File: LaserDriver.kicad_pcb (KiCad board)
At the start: 2 copper layers, 40.2 x 40.5 mm, 30 parts, among them J100 Screw_Terminal_01x04, J101 Screw_Terminal_01x02, J102 nano_left, J103 nano_right, U100 TPS92513DGQR

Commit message: added poors for ground
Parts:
- moved R104 0.83 mm to (49.2, 111.6)
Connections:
- net Net-(C106-Pad1) renamed /intersection
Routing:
- net GND: track 39.1 -> 15.2 mm, vias 18 -> 14
- net /intersection: track 6.43 -> 0.00 mm
- net /ard_DAC: track 4.96 -> 1.94 mm
- net /DAC: track 3.73 -> 2.28 mm
- net Net-(U100-ISENSE): track 2.44 -> 3.26 mm
- added copper zone on F.Cu, net /DAC
- added copper zone on F.Cu, net /ard_DAC
- added copper zone on F.Cu, net /intersection
- added copper zone on F.Cu, net GND

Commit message: added silkscreen and logo
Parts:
- added G***: LOGO, LOGO, F.Cu at (49.6, 125.5)
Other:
- board text added: "DCCD v1.0"
- board text added: "lighteye.ch"

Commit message: created calculator sheets
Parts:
- D101: value D_Zener -> D_Schottky
- moved D101 0.14 mm to (46.0, 104.8)

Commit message: created gerber and assembly files
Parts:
- moved D101 0.25 mm to (46.2, 104.8)
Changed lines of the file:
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@@
 			(usegerberattributes yes)
 			(usegerberadvancedattributes yes)
-			(creategerberjobfile yes)
+			(creategerberjobfile no)
 			(dashed_line_dash_ratio 12.000000)
 			(dashed_line_gap_ratio 3.000000)
@@
 			(outputformat 1)
 			(mirror no)
-			(drillshape 1)
+			(drillshape 0)
 			(scaleselection 1)
-			(outputdirectory "")
+			(outputdirectory "Gerbers/")
 		)
 	)
@@
 	(footprint "Diode_SMD:D_SMB"
 		(layer "F.Cu")
-		(at 46 104.8 90)
+		(at 46.25 104.8 90)
 		(descr "Diode SMB (DO-214AA)")
 		(tags "Diode SMB (DO-214AA)")
@@
 	)
 	(via
-		(at 46.05 99.675)
+		(at 46.3 99.675)
 		(size 1.6)
 		(drill 0.8)
@@
 	)
 	(segment
-		(start 47.31 106.95)
-		(end 49.825 104.435)
+		(start 43.66 106.95)
+		(end 42.825 107.785)
 		(width 0.7)
 		(layer "F.Cu")
@@
 	)
 	(segment
-		(start 46 106.95)
-		(end 43.66 106.95)
+		(start 46.25 106.95)
+		(end 46 107.2)
 		(width 0.7)
 		(layer "F.Cu")
@@
 	)
 	(segment
-		(start 43.66 106.95)
-		(end 42.825 107.785)
+		(start 46 108.626498)
+		(end 45.467501 109.158997)
 		(width 0.7)
 		(layer "F.Cu")
@@
 	)
 	(segment
-		(start 46 106.95)
-		(end 47.31 106.95)
+		(start 47.31 106.95)
+		(end 46.25 106.95)
 		(width 0.7)
 		(layer "F.Cu")
@@
 	)
 	(segment
-		(start 46 106.95)
+		(start 46 107.2)
 		(end 46 108.626498)
 		(width 0.7)
@@
 	)
 	(segment
-		(start 46 108.626498)
-		(end 45.467501 109.158997)
+		(start 49.825 104.435)
+		(end 47.31 106.95)
+		(width 0.7)
+		(layer "F.Cu")
+		(net 4)
+	)
+	(segment
+		(start 46.25 106.95)
+		(end 43.66 106.95)
 		(width 0.7)
 		(layer "F.Cu")
@@
 		(polygon
 			(pts
-				(xy 47.25 104) (xy 44.75 104) (xy 44.75 101.25) (xy 45.5 99.15) (xy 46.55 99.15) (xy 47.25 101.25)
+				(xy 47.5 104) (xy 45 104) (xy 45 101.25) (xy 45.75 99.15) (xy 46.8 99.15) (xy 47.5 101.25)
 			)
 		)

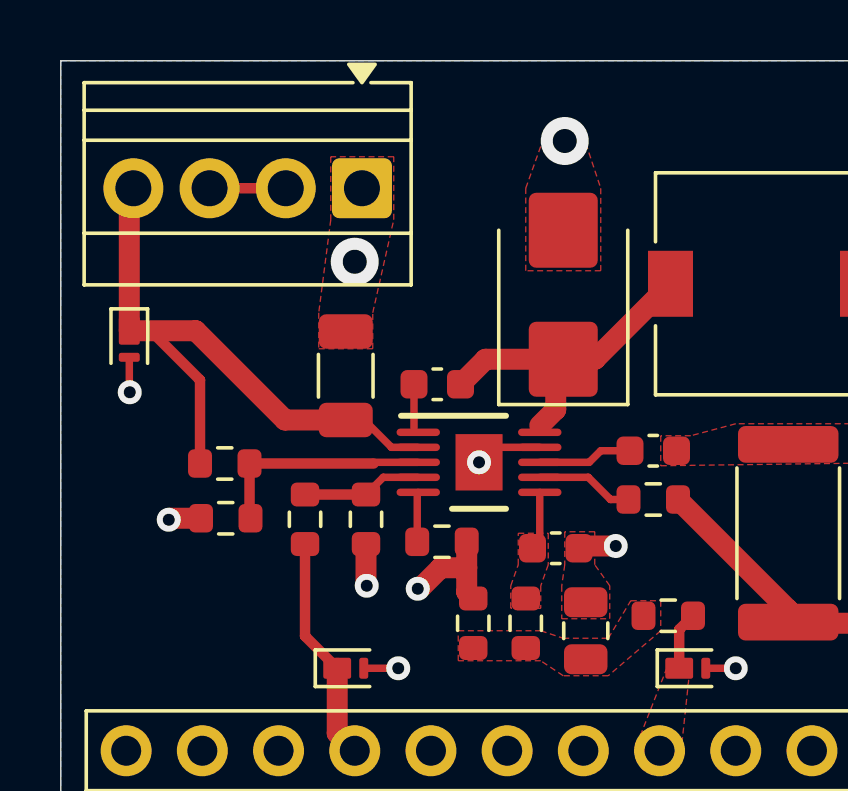
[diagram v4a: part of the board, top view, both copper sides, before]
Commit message: changes to tps ground via
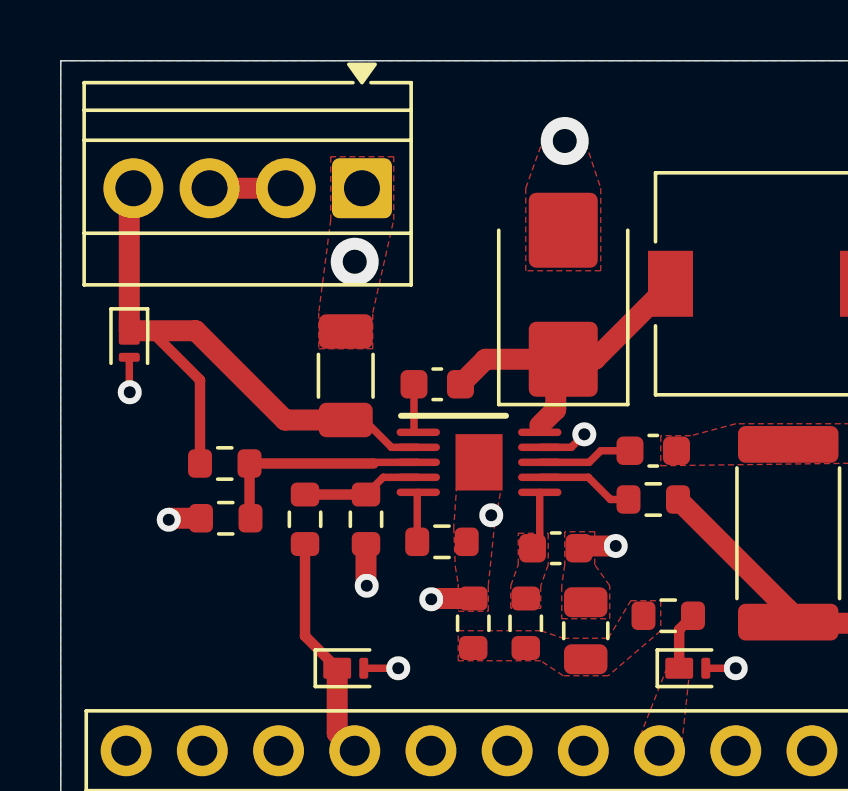
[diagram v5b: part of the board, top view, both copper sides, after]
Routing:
- net GND: track 15.2 -> 12.8 mm, vias 14 -> 15
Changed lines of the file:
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@@
 			(plotpadnumbers no)
 			(hidednponfab no)
-			(sketchdnponfab yes)
-			(crossoutdnponfab yes)
+			(sketchdnponfab no)
+			(crossoutdnponfab no)
 			(subtractmaskfromsilk no)
 			(outputformat 1)
@@
 		)
 		(fp_line
-			(start -0.900001 1.549999)
-			(end 0.900001 1.549999)
-			(stroke
-				(width 0.2)
-				(type solid)
-			)
-			(layer "F.SilkS")
-		)
-		(fp_line
 			(start -2.849999 -1.650002)
 			(end 2.849999 -1.650002)
@@
 	)
 	(segment
-		(start 45.467501 109.884997)
-		(end 43.942503 109.884997)
-		(width 0.25)
-		(layer "F.Cu")
-		(net 1)
-	)
-	(segment
 		(start 31.785 108.035)
 		(end 31.8 108.05)
@@
 	)
 	(segment
-		(start 43.0325 114.7075)
-		(end 43.25 114.925)
-		(width 0.7)
-		(layer "F.Cu")
-		(net 1)
-	)
-	(segment
-		(start 41.4675 114.6)
-		(end 41.4 114.6)
+		(start 48 113.175)
+		(end 46.85 113.175)
 		(width 0.7)
 		(layer "F.Cu")
@@
 	)
 	(segment
-		(start 48 113.175)
-		(end 46.85 113.175)
-		(width 0.7)
+		(start 45.467501 109.884997)
+		(end 46.518987 109.884997)
+		(width 0.25)
 		(layer "F.Cu")
 		(net 1)
@@
 	)
 	(segment
+		(start 41.875 114.925)
+		(end 41.85 114.95)
+		(width 0.7)
+		(layer "F.Cu")
+		(net 1)
+	)
+	(segment
 		(start 64.4 110)
 		(end 63.25 110)
@@
 	)
 	(segment
-		(start 43.0325 113.9)
-		(end 42.1675 113.9)
-		(width 0.7)
+		(start 46.518987 109.884997)
+		(end 46.951992 109.451992)
+		(width 0.25)
 		(layer "F.Cu")
 		(net 1)
@@
 	)
 	(segment
-		(start 42.1675 113.9)
-		(end 41.4675 114.6)
-		(width 0.7)
-		(layer "F.Cu")
-		(net 1)
-	)
-	(segment
-		(start 43.0325 113.9)
-		(end 43.0325 114.7075)
+		(start 43.25 114.925)
+		(end 41.875 114.925)
 		(width 0.7)
 		(layer "F.Cu")
@@
 		(net 1)
 	)
-	(segment
-		(start 43.0325 113.035)
-		(end 43.0325 113.9)
-		(width 0.7)
-		(layer "F.Cu")
-		(net 1)
-	)
 	(via
 		(at 39.3 103.7)
@@
 	)
 	(via
-		(at 43.442501 110.384999)
-		(size 0.8)
-		(drill 0.4)
-		(layers "F.Cu" "B.Cu")
-		(net 1)
-	)
-	(via
 		(at 63.25 110)
 		(size 0.8)
@@
 	)
 	(via
-		(at 41.4 114.6)
+		(at 41.85 114.95)
 		(size 0.8)
 		(drill 0.4)
@@
 	)
 	(via
+		(at 46.951992 109.451992)
+		(size 0.8)
+		(drill 0.4)
+		(layers "F.Cu" "B.Cu")
+		(net 1)
+	)
+	(via
 		(at 52 117.25)
 		(size 0.8)
@@
 		(net 1)
 	)
+	(via
+		(at 43.85 112.15)
+		(size 0.8)
+		(drill 0.4)
+		(layers "F.Cu" "B.Cu")
+		(free yes)
+		(net 1)
+	)
 	(segment
 		(start 50.115 117.25)
@@
 		(start 34.46 101.25)
 		(end 37 101.25)
-		(width 0.35)
+		(width 0.7)
 		(layer "F.Cu")
 		(net 12)
@@
 			)
 		)
+	)
+	(zone
+		(net 1)
+		(net_name "GND")
+		(layer "F.Cu")
+		(hatch edge 0.5)
+		(priority 10)
+		(connect_pads yes
+			(clearance 0.4)
+		)
+		(min_thickness 0.25)
+		(filled_areas_thickness no)
+		(fill yes
+			(thermal_gap 0.5)
+			(thermal_bridge_width 0.5)
+		)
+		(polygon
+			(pts
+				(xy 42.7 111.15) (xy 42.6 112.55) (xy 42.65 113.85) (xy 42.75 114.45) (xy 42.75 115.35) (xy 43.75 115.35)
+				(xy 43.75 114.5) (xy 43.85 113.55) (xy 43.95 112.55) (xy 44.2 111.15)
+			)
+		)

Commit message: finished BOM
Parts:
- D100: value PTVS12VZ1USK -> PTVS20VZ1USK
- D102, D103, D104: value PTVS5V0Z1USK -> PTVS10VZ1USK
- moved D103 11.4 mm to (50.4, 117.2)
- moved D104 11.4 mm to (39.0, 117.2)
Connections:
- D103 pad 1: /ard_PWM -> /ard_DAC
- D104 pad 1: /ard_DAC -> /ard_PWM
